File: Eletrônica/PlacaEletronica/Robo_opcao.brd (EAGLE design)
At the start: 139.7 x 153.7 mm, 114 parts, among them IC1 7805DT, IC2 7805DT, J1 PJ-002A, J3 ZX62-B-5PA, J4 F-1X06-SIP-100-40, Q1 SMD-TRANSISTORS-NPN-25V-500MW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, Q2 SMD-TRANSISTORS-NPN-25V-500MW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, Q4 SFH_3716, Q5 TSOP4838, U1 ESP32-WROOM-32D, U2 AMS1117-3.3, U3 INTERFACE-CP2102-GMR(QFN28)QF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

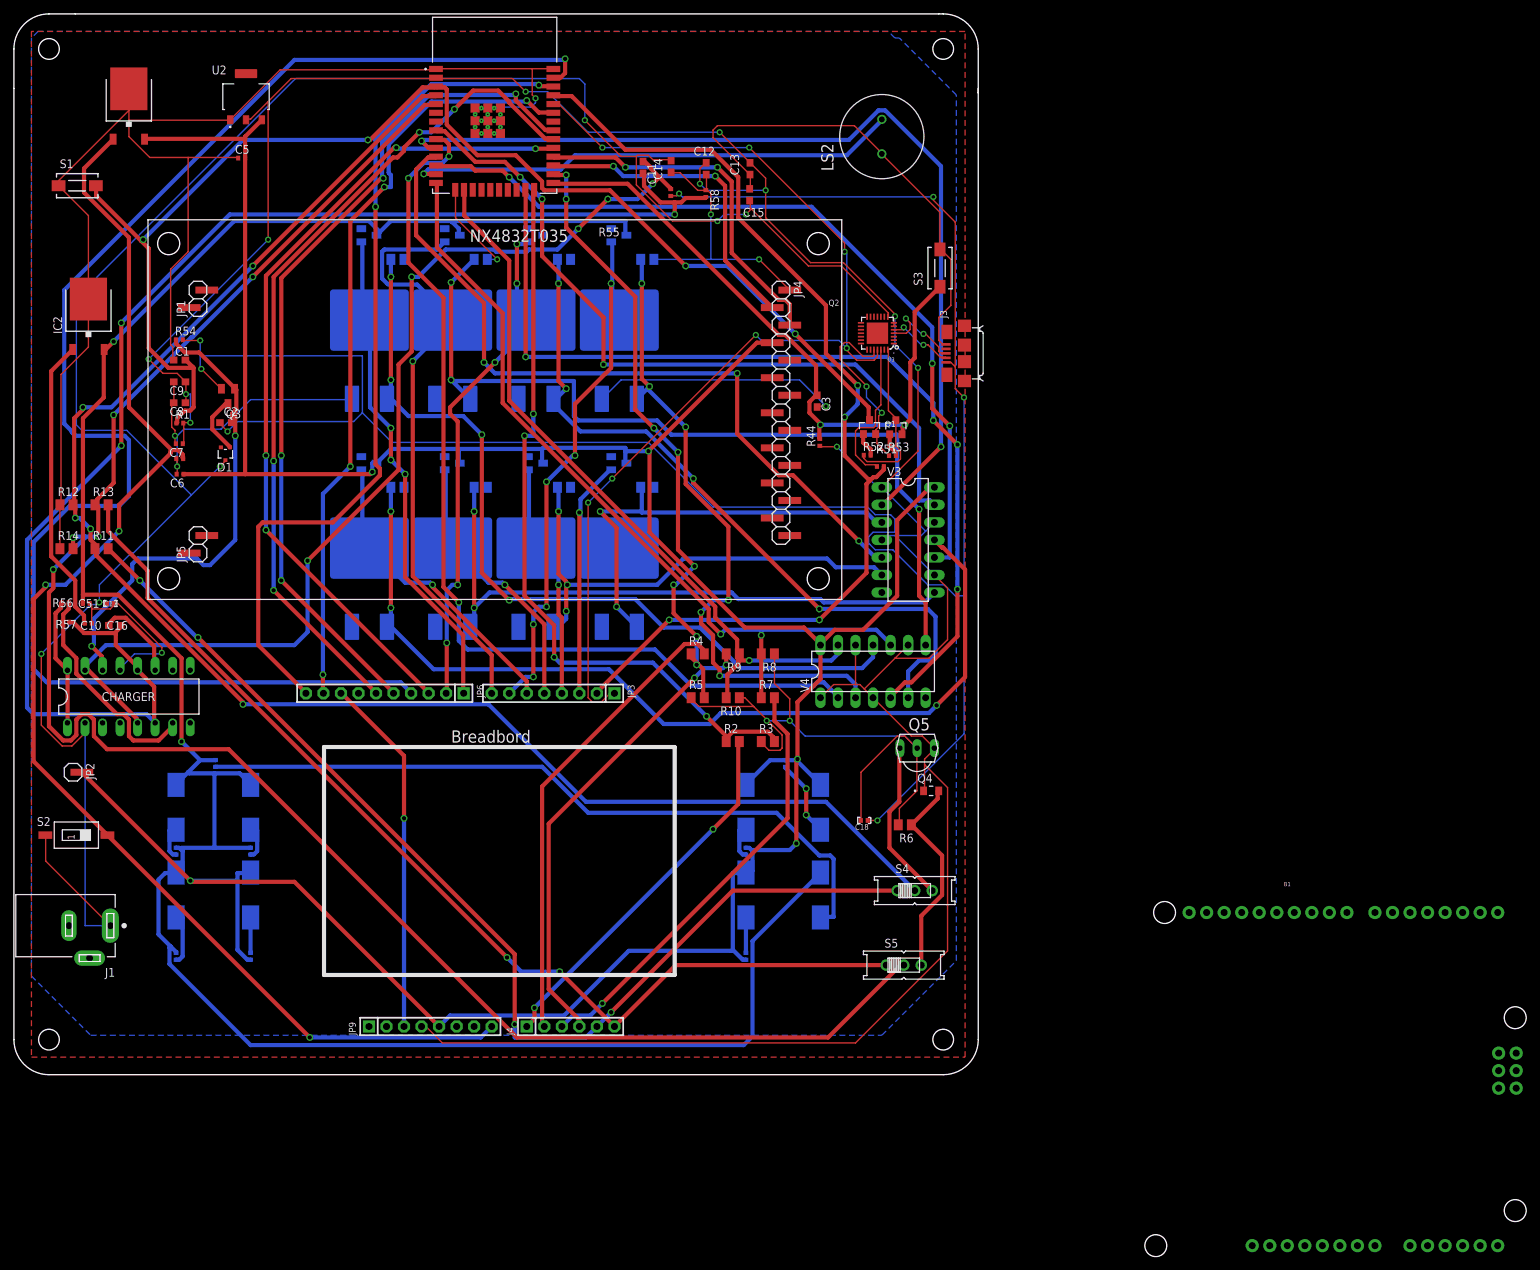
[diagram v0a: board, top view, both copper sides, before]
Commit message: [MODIFIED] Botoes Maiores e Troca do Regulador de Tensao
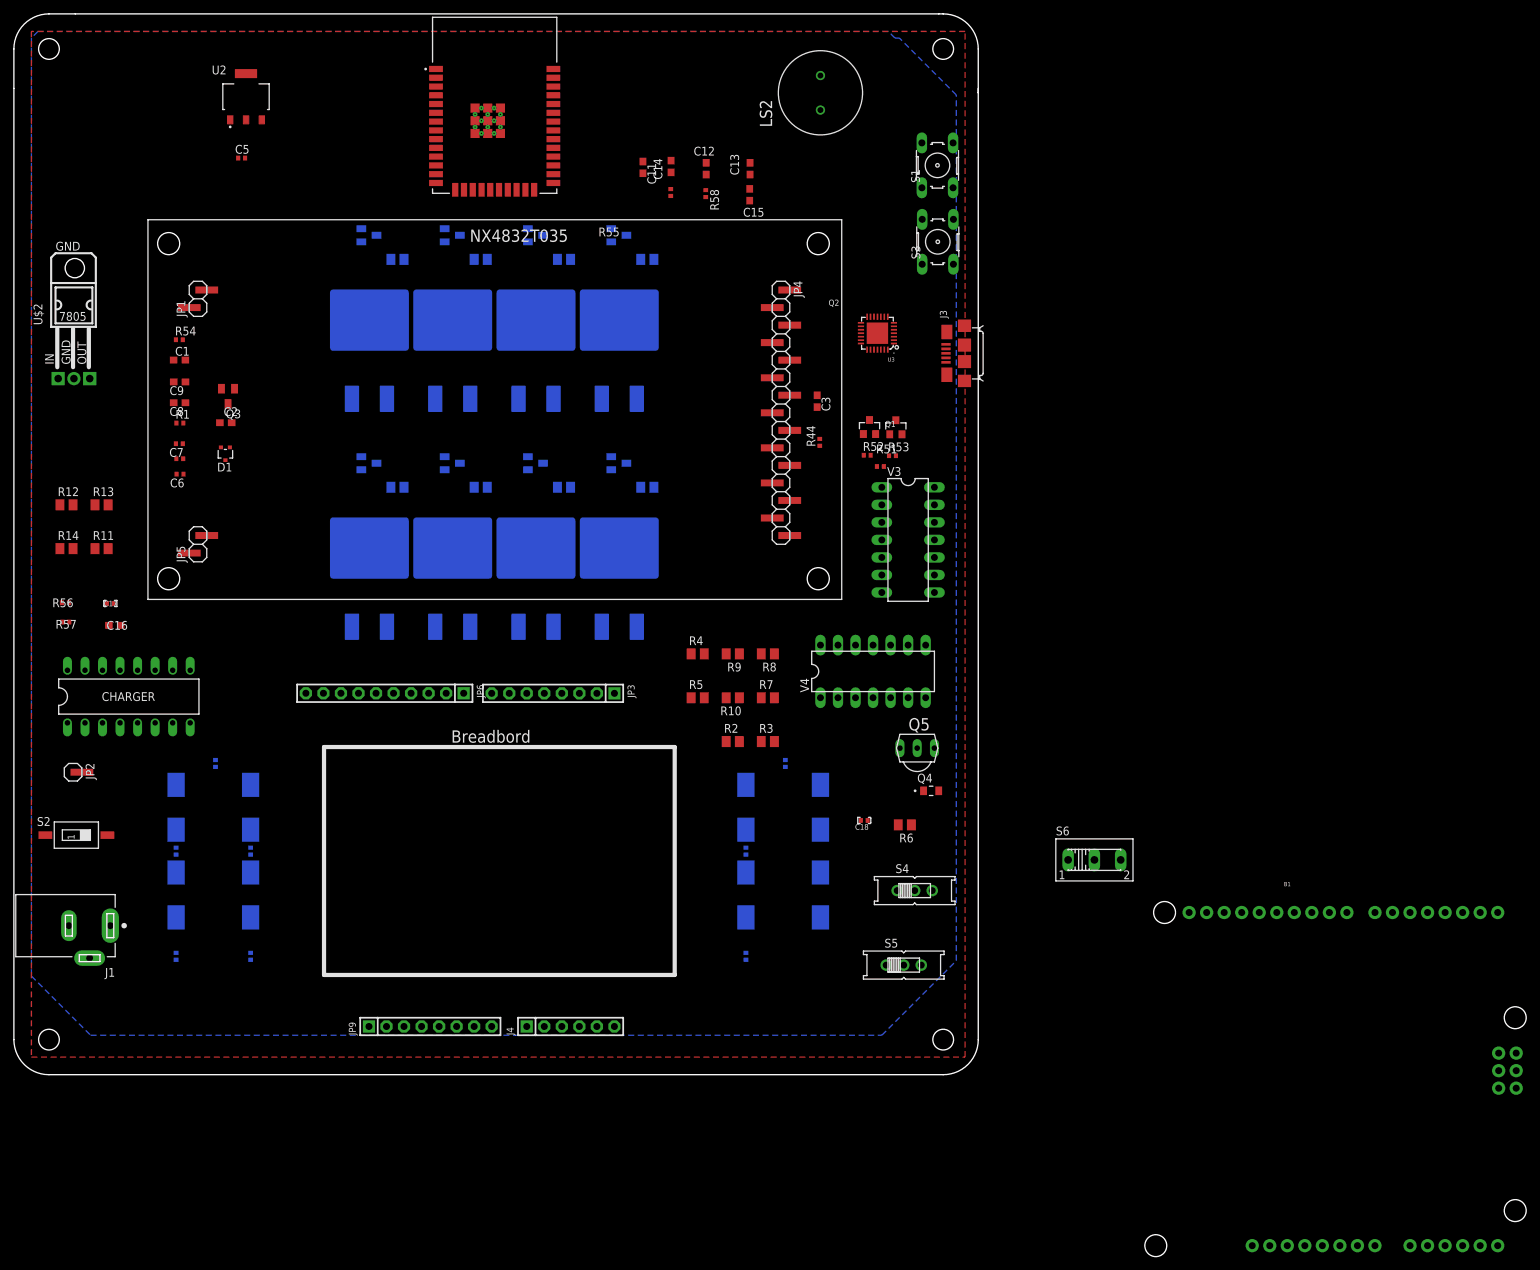
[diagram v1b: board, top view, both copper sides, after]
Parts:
- removed C10: 0.33uF, Perfect_0402:0402
- removed C51: 0.1uF, Perfect_0402:0402
- removed IC1, IC2: 7805DT, linear:TO252
- added S6: (no value), switch:255SB
- added U$2: -L7805, tango:L7805
- S1, S3: device switch-tact:DTSM-3 -> switch-omron:B3F-10XX
- moved S1 124.7 mm to (133.8, 131.7), turned to 90 degrees
- moved LS2 10.9 mm to (116.8, 142.2)
- moved S3 3.82 mm to (133.8, 120.7)
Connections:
- removed net GND_PWM~5V1(2): C42.2, C43.+, C44.2, C45.+, C46.2, C47.+, C48.2, C49.+, C51.2, D14.3, D15.3, D16.3, D17.3, IC2.2
- removed net VIN1: C10.2, IC2.1
- net EN: now also S1.1; no longer S1.2
- net GND: now also S1.3, S3.1, U$2.GND; no longer C10.1, C51.1, IC1.3, IC2.3, S1.1, S3.2
- net GND_MOSFET: now also C42.2, C43.+, C44.2, C45.+, C46.2, C47.+, C48.2, C49.+, D14.3, D15.3, D16.3, D17.3, U$2.OUT; no longer IC1.2
- net IO0: now also S3.3; no longer S3.1
- net VIN: now also U$2.IN; no longer IC1.1
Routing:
- net GND: track 529.3 -> 0.00 mm, vias 10 -> 0
- net GND_MOSFET: track 452.1 -> 0.00 mm, vias 5 -> 0
- net VDD33: track 430.8 -> 0.00 mm, vias 11 -> 0
- net GND_PWM~5V1(2): track 342.5 -> 0.00 mm, vias 2 -> 0
- net DC_IN: track 311.4 -> 0.00 mm, vias 7 -> 0
- net B+: track 309.7 -> 0.00 mm, vias 6 -> 0
- net VN_SENSOR: track 272.1 -> 0.00 mm, vias 5 -> 0
- net VP_SENSOR: track 232.6 -> 0.00 mm, vias 5 -> 0
- net IO23-SPI: track 219.5 -> 0.00 mm, vias 1 -> 0
- net B-: track 205.7 -> 0.00 mm, vias 3 -> 0
- net VIN: track 193.1 -> 0.00 mm, vias 3 -> 0
- net EN: track 184.8 -> 0.00 mm, vias 4 -> 0
- net VP_SENSOR_IN: track 159.5 -> 0.00 mm, vias 4 -> 0
- net RX0: track 153.7 -> 0.00 mm, vias 7 -> 0
- net VN_SENSOR_IN: track 152.3 -> 0.00 mm, vias 2 -> 0
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
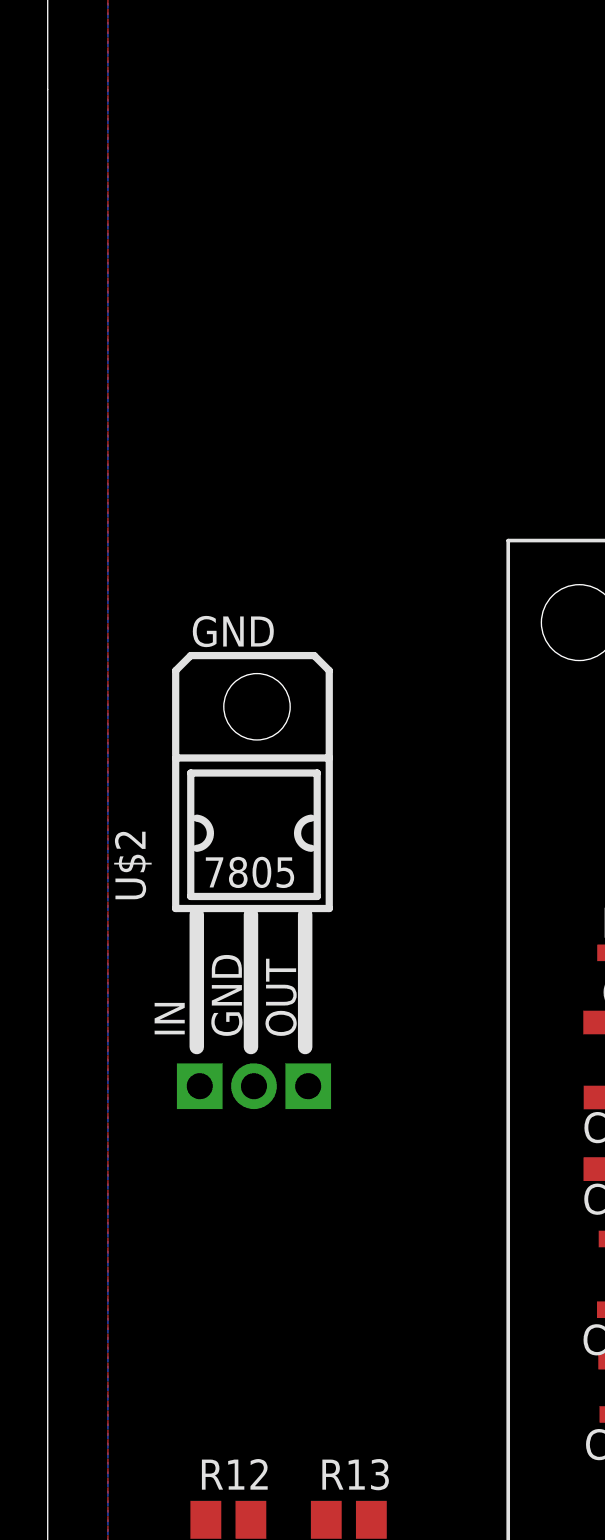
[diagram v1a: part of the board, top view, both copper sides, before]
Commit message: [MODIFIED] Regulador de tensao em paralelo
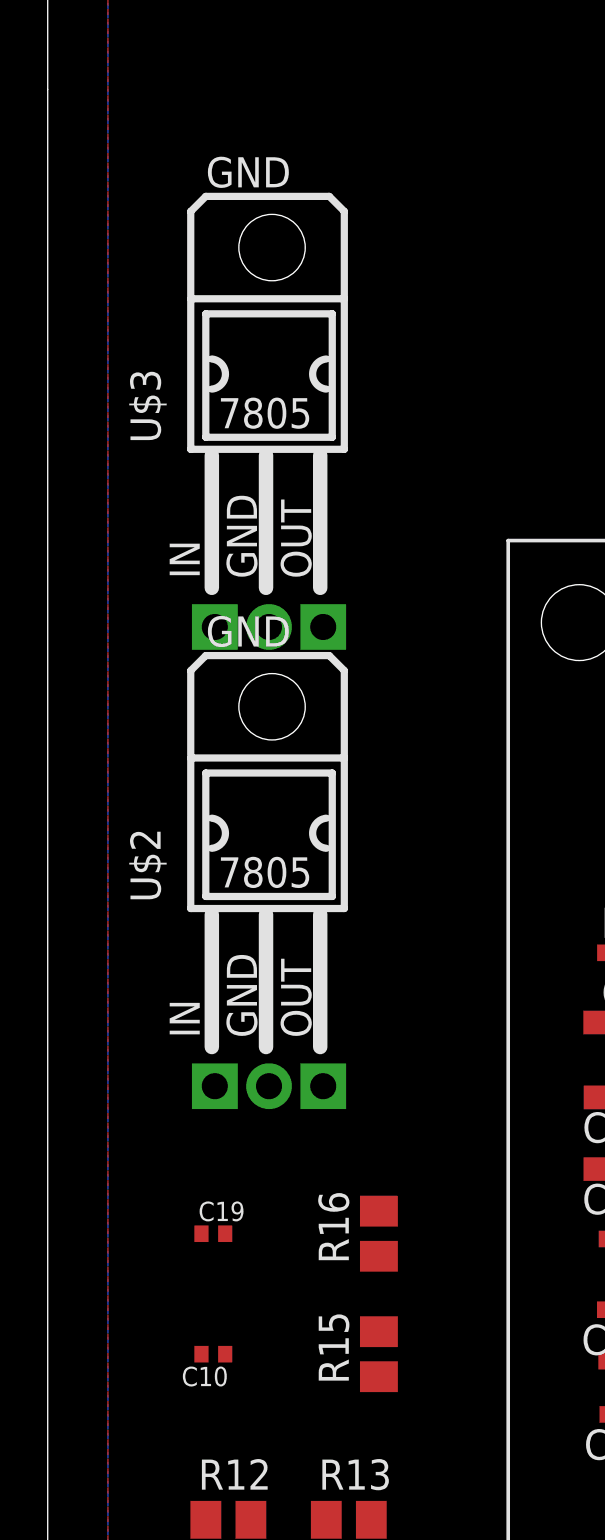
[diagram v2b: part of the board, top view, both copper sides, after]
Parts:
- added C10: 0.33uF, Perfect_0402:0402
- added C19: 0.1uF, Perfect_0402:0402
- added R15, R16: 0.47, rcl:M0805
- added U$3: -L7805, tango:L7805
- moved U$2 0.63 mm to (9.21, 110.5)
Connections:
- new net N$1: C19.2, R15.1, U$3.OUT
- new net N$2: C5.2, R16.2, U$2.OUT
- net GND: now also C10.1, C19.1, U$3.GND
- net GND_MOSFET: now also R15.2, R16.1; no longer C5.2, U$2.OUT
- net VIN: now also C10.2, U$3.IN

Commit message: [MODIFIED] Pinos do Engino
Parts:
- removed JP2: (no value), pinhead-1:1X01SMD
- moved B1 131.9 mm to (56.4, 31.2)
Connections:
- removed net GND_MOSFET: C34.2, C35.+, C36.2, C37.+, C38.2, C39.+, C40.2, C41.+, C42.2, C43.+, C44.2, C45.+, C46.2, C47.+, C48.2, C49.+, C6.1, D10.3, D11.3, D12.3, D13.3, D14.3, D15.3, D16.3, D17.3, JP2.1, JP4.4, JP9.5, R15.2, R16.1, U2.3, V3.14, V4.14
- new net GND_MOSFET~5V: C34.2, C35.+, C36.2, C37.+, C38.2, C39.+, C40.2, C41.+, C42.2, C43.+, C44.2, C45.+, C46.2, C47.+, C48.2, C49.+, C6.1, D10.3, D11.3, D12.3, D13.3, D14.3, D15.3, D16.3, D17.3, JP4.4, JP9.5, R15.2, R16.1, U2.3, V3.14, V4.14
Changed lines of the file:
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@@
 <setting verticaltext="up"/>
 </settings>
-<grid distance="25" unitdist="mil" unit="mil" style="lines" multiple="1" display="yes" altdistance="5" altunitdist="mil" altunit="mil"/>
+<grid distance="6.125" unitdist="mil" unit="mil" style="lines" multiple="1" display="yes" altdistance="5" altunitdist="mil" altunit="mil"/>
 <layers>
 <layer number="1" name="Top" color="4" fill="1" visible="yes" active="yes"/>
@@
 <attribute name="VALUE" x="71.755" y="5.715" size="0.8128" layer="27" ratio="10" rot="R90"/>
 </element>
-<element name="B1" library="SparkFun-Boards" library_urn="urn:adsk.eagle:library:509" package="ARDUINO_R3" package3d_urn="urn:adsk.eagle:package:37330/1" value="ARDUINO_UNO_R3" x="184.4675" y="-0.635" smashed="yes">
-<attribute name="NAME" x="184.4675" y="27.305" size="0.6096" layer="25" font="vector" ratio="20" align="bottom-center"/>
-<attribute name="VALUE" x="184.4675" y="-28.575" size="0.6096" layer="27" font="vector" ratio="20" align="top-center"/>
+<element name="B1" library="SparkFun-Boards" library_urn="urn:adsk.eagle:library:509" package="ARDUINO_R3" package3d_urn="urn:adsk.eagle:package:37330/1" value="ARDUINO_UNO_R3" x="56.441975" y="31.213425" smashed="yes">
+<attribute name="NAME" x="56.441975" y="59.153425" size="0.6096" layer="25" font="vector" ratio="20" align="bottom-center"/>
+<attribute name="VALUE" x="56.441975" y="3.273425" size="0.6096" layer="27" font="vector" ratio="20" align="top-center"/>
 </element>
 <element name="J1" library="PJ-002A" package="CUI_PJ-002A" value="PJ-002A" x="13.97" y="21.59" smashed="yes" rot="R180">
@@
 <attribute name="SPICEPREFIX" value="R" x="7.62" y="63.5" size="1.778" layer="27" display="off"/>
 <attribute name="VALUE" x="6.35" y="73.66" size="1.27" layer="27"/>
-</element>
-<element name="JP2" library="pinhead-1" package="1X01SMD" value="" x="8.5725" y="42.545" smashed="yes" rot="R270">
-<attribute name="NAME" x="10.4013" y="45.1612" size="1.27" layer="25" ratio="10" rot="R270"/>
-<attribute name="VALUE" x="5.3975" y="45.085" size="1.27" layer="27" rot="R270"/>
 </element>
 <element name="U$2" library="tango" package="L7805" value="-L7805" x="9.2075" y="110.49" smashed="yes">
@@
 <vertex x="2.54" y="150.1775"/>
 <vertex x="2.54" y="14.2875"/>
-<vertex x="11.1125" y="5.715"/>
-<vertex x="125.73" y="5.715"/>
+<vertex x="13.6525" y="3.175"/>
+<vertex x="123.19" y="3.175"/>
 <vertex x="136.525" y="16.51"/>
 <vertex x="136.525" y="141.9225"/>
@@
 <contactref element="C16" pad="2"/>
 </signal>
-<signal name="GND_MOSFET">
+<signal name="GND_MOSFET~5V">
 <contactref element="V3" pad="14"/>
 <contactref element="V4" pad="14"/>
@@
 <contactref element="C41" pad="+"/>
 <contactref element="JP4" pad="4"/>
-<contactref element="JP2" pad="1"/>
 <contactref element="JP9" pad="5"/>
 <contactref element="D14" pad="3"/>
@@
 <wire x1="52.535" y1="88.5825" x2="64.6" y2="88.5825" width="0" layer="19" extent="16-16"/>
 <wire x1="24.57285" y1="86.991825" x2="52.535" y2="88.5825" width="0" layer="19" extent="1-16"/>
+<wire x1="13.97" y1="90.485" x2="24.57285" y2="86.991825" width="0" layer="19" extent="1-1"/>
+<wire x1="13.97" y1="93.665" x2="13.97" y2="90.485" width="0" layer="19" extent="1-1"/>
 <wire x1="29.21" y1="45.585" x2="24.57285" y2="86.991825" width="0" layer="19" extent="1-16"/>
 <wire x1="34.29" y1="41.985" x2="29.21" y2="45.585" width="0" layer="19" extent="16-16"/>
@@
 <wire x1="23.495" y1="17.645" x2="23.495" y2="29.285" width="0" layer="19" extent="16-16"/>
 <wire x1="34.29" y1="16.645" x2="23.495" y2="17.645" width="0" layer="19" extent="16-16"/>
-<wire x1="9.8425" y1="43.815" x2="23.495" y2="41.985" width="0" layer="19" extent="1-16"/>
 <wire x1="61.595" y1="6.985" x2="34.29" y2="16.645" width="0" layer="19" extent="16-16"/>
-<wire x1="13.97" y1="90.485" x2="23.495" y2="17.645" width="0" layer="19" extent="1-16"/>
-<wire x1="13.97" y1="93.665" x2="13.97" y2="90.485" width="0" layer="19" extent="1-1"/>
 </signal>
 <signal name="N$28">
@@
 <contactref element="J4" pad="6"/>
 <contactref element="R13" pad="2"/>
+<wire x1="86.995" y1="6.985" x2="126.365" y2="15.875" width="0" layer="19" extent="1-1"/>
+<wire x1="13.65" y1="82.55" x2="86.995" y2="6.985" width="0" layer="19" extent="1-1"/>
 </signal>
 <signal name="VP_SENSOR_IN">
@@
 <contactref element="J4" pad="5"/>
 <contactref element="R11" pad="2"/>
+<wire x1="84.455" y1="6.985" x2="127.9525" y2="26.67" width="0" layer="19" extent="1-1"/>
+<wire x1="13.65" y1="76.2" x2="84.455" y2="6.985" width="0" layer="19" extent="1-1"/>
 </signal>
 <signal name="VN_SENSOR_LDR">
